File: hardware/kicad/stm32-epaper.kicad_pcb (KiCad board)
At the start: 4 copper layers, 97.4 x 60 mm, 155 parts, among them J1 USB_C_Receptacle_USB2.0_16P, J101 TC2050-IDC-NL, J102 UART (TX RX GND), J2 BATT (1S LiPo), J201 microSD, J301 IT8951 HAT, J302 Electrodes L, J303 Electrodes R, SW101 BOOT, SW301 PEC11R-4220F-S0024, SW302 POWER, U1 BQ24073RGT, U101 STM32F469IIT6, U2 TPS63802DLA, U201 IS42S16400J-6TLI, U202 W25Q128JVSIQ, U3 TPS61023DRL, U301 CAP1188-1-CP-TR, U302 TPD4E05U06DQAR, U4 TPS22965DSG, U5 USBLC6-2SC6, U6 TPS63900DSK, U7 MCP1700T-3002E/TT, Y101 8MHz CL8pF, Y102 32.768kHz CL6pF

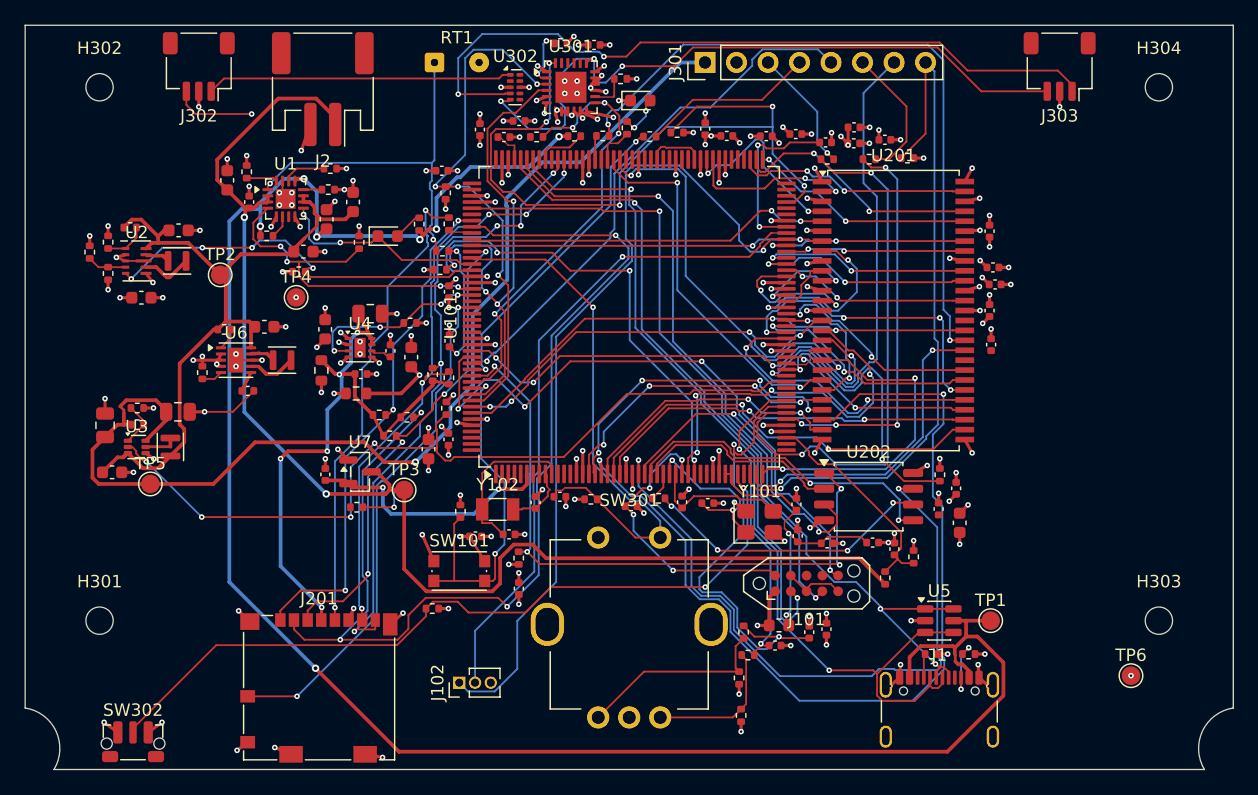
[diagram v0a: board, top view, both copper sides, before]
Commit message: Routing attempt 9: 12 unconnected (best); left touch pair routes via the CAP1188 corridor
Best-of-N parallel freerouting option added to route_loop.py.

Co-Authored-By: Claude Opus 5.5 <noreply@anthropic.com>
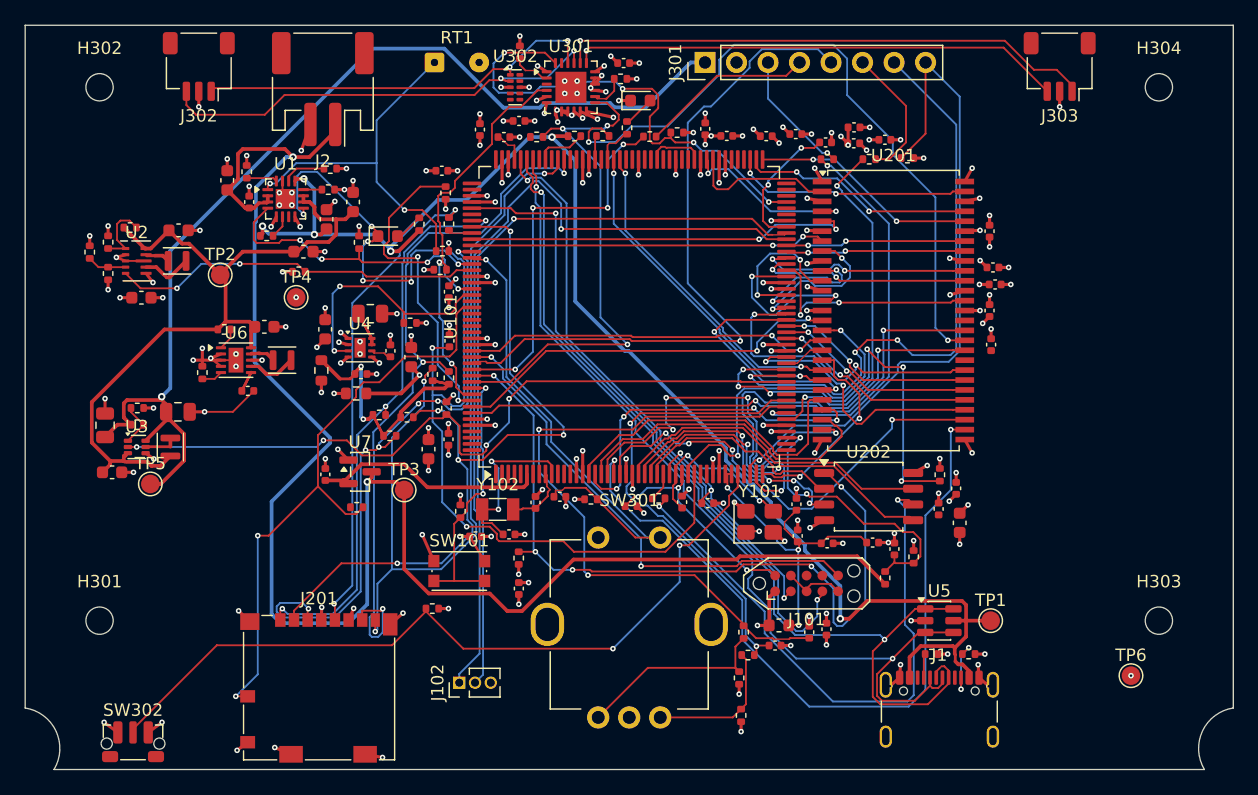
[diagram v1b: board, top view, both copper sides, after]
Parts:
- moved R308 3.36 mm to (139.9, 102.2), turned to 90 degrees
- moved C301 2.79 mm to (148.2, 103.0)
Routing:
- net FMC_A2: track 74.9 -> 26.1 mm, vias 2 -> 0
- net VBUS: track 162.7 -> 115.4 mm, vias 7 -> 6
- net /Peripherals/TOUCH_L2: track 6.67 -> 36.7 mm, vias 1 -> 2
- net QUADSPI_BK1_IO3: track 54.4 -> 26.3 mm, vias 2 -> 0
- net +BATT: track 104.6 -> 132.5 mm
- net FMC_A4: track 33.9 -> 61.7 mm
- net 3V3_PERIPH: track 75.2 -> 47.9 mm, vias 23 -> 21
- net SDIO_D3: track 89.2 -> 62.0 mm, vias 4 -> 5
- net QSPI_FLASH_CLK: track 23.6 -> 46.8 mm, vias 4 -> 2
- net CAP_RESET: track 60.4 -> 39.7 mm, vias 5 -> 4
- net ENC_A: track 36.4 -> 54.2 mm
- net /Peripherals/TOUCH_R1: track 60.6 -> 43.4 mm, vias 2 -> 1
- net I2C1_SDA: track 42.7 -> 25.7 mm, vias 4 -> 2
- net /Peripherals/TOUCH_R2: track 56.3 -> 39.7 mm, vias 3 -> 1
- net SDIO_D1: track 51.2 -> 66.5 mm, vias 5 -> 3
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
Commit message: Routing attempt 10: 11 unconnected, 0 clearance errors, SDIO/QSPI rules pass
Pre-router uses the real net-class clearances; U4 on the +3V3/3V3_PERIPH
zone boundary. Best-of-3 gave identical runs: freerouting is deterministic
for a given DSN.

Co-Authored-By: Claude Opus 5.5 <noreply@anthropic.com>
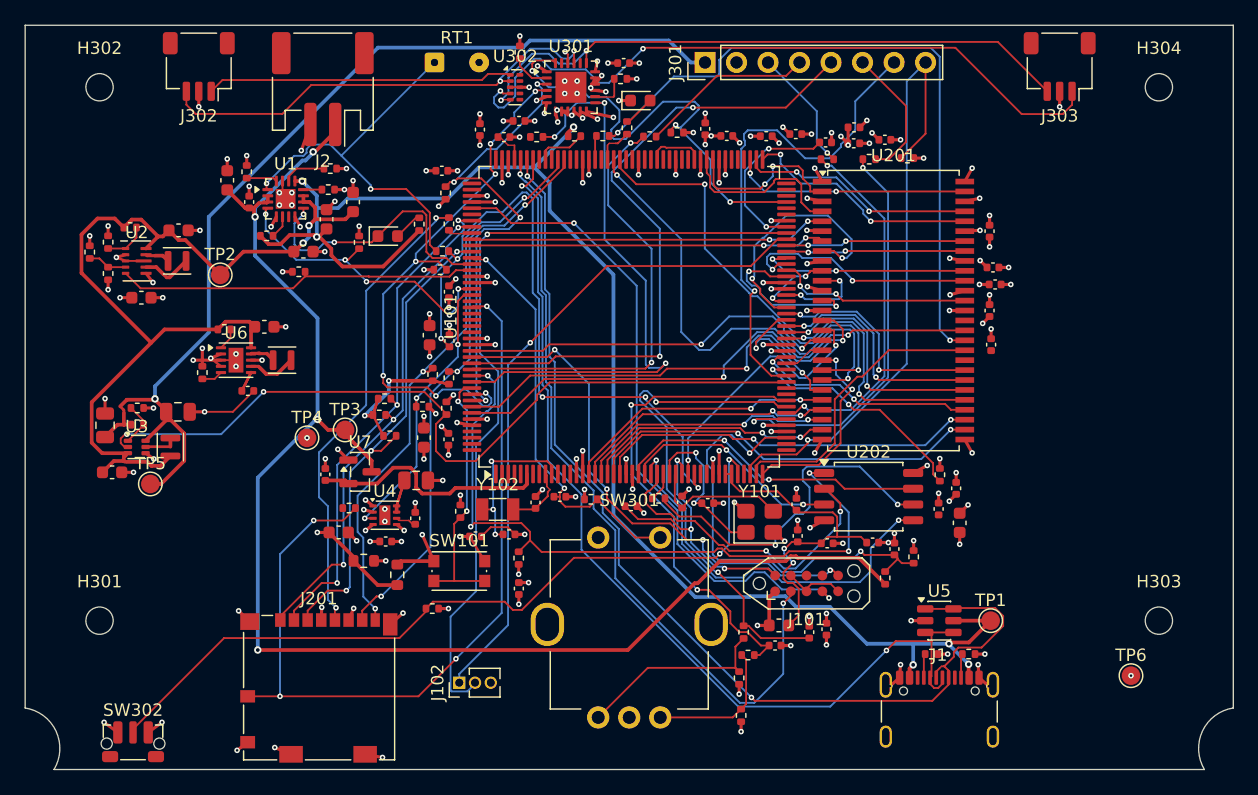
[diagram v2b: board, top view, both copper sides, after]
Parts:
- moved C9 16.4 mm to (125.3, 140.9), turned to 0 degrees
- moved R13 15.7 mm to (127.3, 143.2), turned to 0 degrees
- moved R18 15.0 mm to (130.0, 144.3), turned to 90 degrees
- moved C208 13.9 mm to (131.5, 136.7)
- moved C14 13.6 mm to (131.4, 139.8)
- moved U4 13.6 mm to (129.0, 139.5)
- moved C209 13.6 mm to (129.1, 141.6)
- moved TP4 11.4 mm to (122.7, 133.3)
- moved R14 6.82 mm to (132.0, 130.8)
- moved TP3 6.79 mm to (125.8, 132.6)
- moved R206 2.35 mm to (129.0, 130.1)
- moved C114 2.31 mm to (132.6, 125.0)
- moved C7 1.00 mm to (132.2, 133.2)
- moved R207 0.62 mm to (126.1, 138.9)
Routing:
- net FMC_A4: track 61.7 -> 32.4 mm
- net SDIO_D3: track 62.0 -> 39.7 mm, vias 5 -> 3
- net SDIO_D1: track 66.5 -> 46.3 mm
- net SD_DETECT: track 48.8 -> 68.8 mm, vias 2 -> 4
- net QSPI_FLASH_CLK: track 46.8 -> 28.7 mm
- net /MCU/SWDIO: track 45.9 -> 62.6 mm
- net /MCU/BOOT1: track 35.1 -> 18.8 mm, vias 6 -> 2
- net +BATT: track 132.5 -> 116.2 mm, vias 2 -> 4
- net ENC_A: track 54.2 -> 40.5 mm
- net /Peripherals/TOUCH_R1: track 43.4 -> 56.9 mm, vias 1 -> 2
- net I2C1_SDA: track 25.7 -> 38.6 mm, vias 2 -> 4
- net /MCU/USART3_TX: track 66.8 -> 53.9 mm
- net SDIO_D0: track 58.9 -> 46.1 mm
- net FMC_SDCKE0: track 36.1 -> 23.4 mm, vias 2 -> 0
- net I2C1_SCL: track 32.2 -> 44.8 mm, vias 2 -> 7
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
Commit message: Routing attempt 12: 5 unconnected - plane-aware placement
Parts on one 3.3 V rail are only placed over that rail's In2 plane
(C104/C105/R207/C208 had landed over the wrong island), 3.5 mm
MCU-memory gap for decoupling caps, memory-island edge from placement,
decoupling falls back to its own IC. SDRAM lengths got longer (gap).

Co-Authored-By: Claude Opus 5.5 <noreply@anthropic.com>
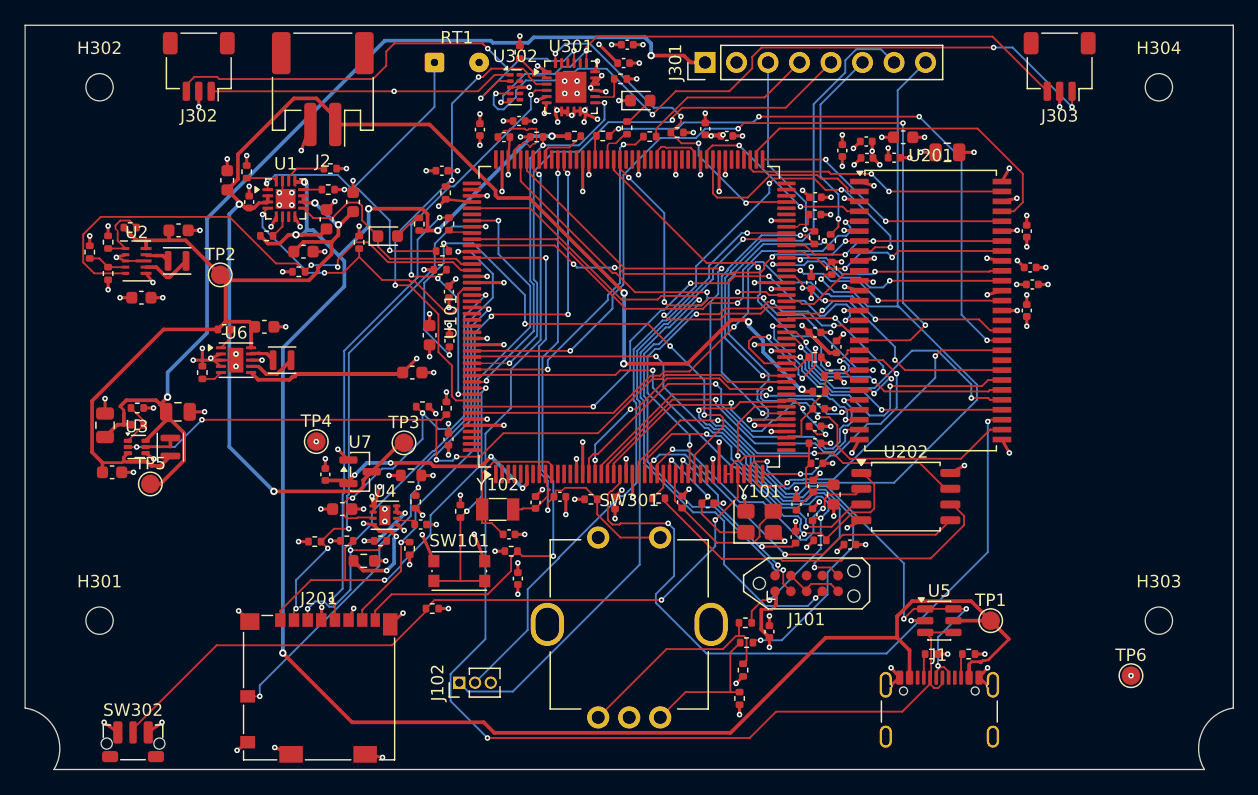
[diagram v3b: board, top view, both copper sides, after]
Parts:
- moved C209 56.5 mm to (181.0, 119.5)
- moved C208 50.3 mm to (174.3, 110.2)
- moved C302 41.4 mm to (148.5, 101.6)
- moved C210 31.4 mm to (170.8, 109.0), turned to 0 degrees
- moved R201 24.3 mm to (164.1, 141.5), turned to 0 degrees
- moved C304 18.0 mm to (163.7, 132.3)
- moved R22 16.1 mm to (165.0, 128.2), turned to 0 degrees
- moved R21 15.9 mm to (164.0, 129.5), turned to 0 degrees
- moved R204 15.6 mm to (139.2, 142.4), turned to 0 degrees
- moved C104 15.4 mm to (165.4, 125.9)
- moved C211 14.4 mm to (167.8, 109.4)
- moved C105 14.2 mm to (163.7, 124.8), turned to 0 degrees
- moved R203 14.1 mm to (131.0, 142.2)
- moved R102 13.8 mm to (163.7, 126.8), turned to 0 degrees
- moved C126 13.5 mm to (162.1, 141.3), turned to 90 degrees
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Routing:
- net FMC_SDNCAS: track 30.9 -> 71.0 mm, vias 2 -> 4
- net 3V3_AON: track 59.9 -> 95.3 mm, vias 40 -> 45
- net VBUS: track 122.3 -> 155.5 mm
- net VBAT_SENSE: track 36.0 -> 6.96 mm, vias 2 -> 0
- net FMC_A5: track 31.1 -> 60.0 mm
- net SD_DETECT: track 68.8 -> 42.2 mm, vias 4 -> 3
- net FMC_D4: track 20.3 -> 40.1 mm, vias 2 -> 4
- net USB_DM: track 78.1 -> 97.0 mm
- net FMC_SDNRAS: track 3.31 -> 20.8 mm, vias 0 -> 4
- net CAP_ALERT: track 48.0 -> 30.9 mm
- net /MCU/BOOT1: track 18.8 -> 2.20 mm, vias 2 -> 0
- net /MCU/USART3_RX: track 65.7 -> 49.3 mm
- net QUADSPI_BK1_NCS: track 57.1 -> 44.2 mm, vias 4 -> 2
- net 3V3_PG: track 29.4 -> 42.2 mm, vias 0 -> 2
- net USB_DP: track 84.0 -> 71.6 mm, vias 2 -> 4
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
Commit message: Routing attempt 13: 3 unconnected - CAP1188 inputs reassigned, ESD per connector
Left electrodes on CS3/CS4, right on CS5/CS6 (CS1-4 all on the top side
fenced in the VDD pin); U302/U303 TPD2E2U06 right at J302/J303 replace the
single TPD4E05U06.

Co-Authored-By: Claude Opus 5.5 <noreply@anthropic.com>
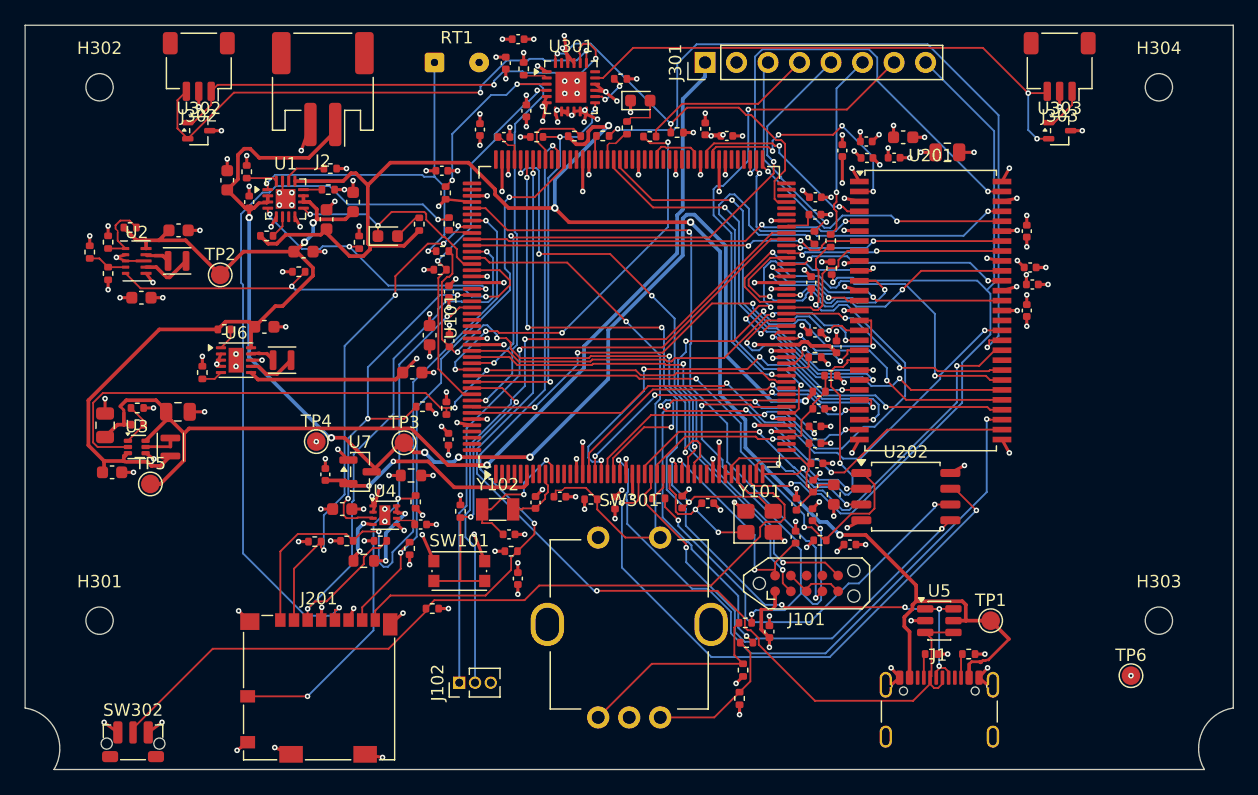
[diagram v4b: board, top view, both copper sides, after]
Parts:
- added U303: TPD2E2U06DCKR, Package_TO_SOT_SMD:SOT-323_SC-70, F.Cu at (183.4, 108.5)
- U302: value TPD4E05U06DQAR -> TPD2E2U06DCKR; footprint Package_SON:USON-10_2.5x1.0mm_P0.5mm -> Package_TO_SOT_SMD:SOT-323_SC-70
- moved U302 25.7 mm to (114.0, 108.5)
- moved C302 9.91 mm to (138.8, 103.0), turned to 90 degrees
- moved C301 8.72 mm to (139.7, 101.1)
- moved R308 1.37 mm to (140.2, 103.5)
- moved C110 1.00 mm to (140.4, 106.9), turned to 90 degrees
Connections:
- U301 pad 17: GND -> /Peripherals/TOUCH_R2
- U301 pad 18: GND -> /Peripherals/TOUCH_R1
- U301 pad 19: /Peripherals/TOUCH_R2 -> /Peripherals/TOUCH_L2
- U301 pad 20: /Peripherals/TOUCH_R1 -> /Peripherals/TOUCH_L1
- U301 pad 21: /Peripherals/TOUCH_L2 -> GND
- U301 pad 22: /Peripherals/TOUCH_L1 -> GND
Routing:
- net /Peripherals/TOUCH_R1: track 58.2 -> 3.57 mm, vias 4 -> 0
- net FMC_SDNCAS: track 71.0 -> 34.6 mm, vias 4 -> 2
- net FMC_D4: track 40.1 -> 9.73 mm, vias 4 -> 0
- net VBUS: track 155.5 -> 131.3 mm, vias 6 -> 4
- net SDCARD_CLK: track 36.9 -> 57.6 mm
- net QUADSPI_BK1_IO3: track 29.8 -> 48.0 mm
- net USB_DM: track 97.0 -> 81.0 mm
- net FMC_D15: track 21.8 -> 36.7 mm
- net /Peripherals/TOUCH_L1: track 24.7 -> 39.5 mm, vias 1 -> 2
- net SDRAM_CLK: track 47.1 -> 60.6 mm, vias 4 -> 2
- net FMC_SDNRAS: track 20.8 -> 7.59 mm, vias 4 -> 2
- net FMC_A9: track 25.6 -> 36.7 mm, vias 2 -> 4
- net FMC_D5: track 7.07 -> 17.7 mm, vias 0 -> 2
- net 3V3_AON: track 95.3 -> 85.3 mm
- net ENC_A: track 30.0 -> 39.6 mm
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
